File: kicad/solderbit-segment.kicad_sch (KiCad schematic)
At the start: 13 parts, among them J1 Conn_01x05_Pin, U1 PCF8574AT, U2 PCF8574N

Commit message: Update schematic and cleanup
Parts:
- C1: Onecall order code (none) -> 3188966; Package (none) -> 1206
- DS1: value ADMR10A0 -> ADMO10A0; Onecall order code (none) -> 2682705; Package (none) -> 10mm,SMD
- J1: Onecall CN14490 -> (none); Onecall order code (none) -> CN14490; Package (none) -> 2.54mm,THT
- R1, R2, R3, R4, R5, R6, R7, R8: value 220R -> 150R; Onecall order code (none) -> 9240420RL; Package (none) -> 1206
- U1: Onecall 2776146 -> (none); Onecall order code (none) -> 2776146; now not fitted
- U2: Onecall 3124747 -> (none); Onecall order code (none) -> 3124747
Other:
- moved on the sheet: C1, DS1, J1, R1, R2, R3, R4, R5, R6, R7, R8, U2

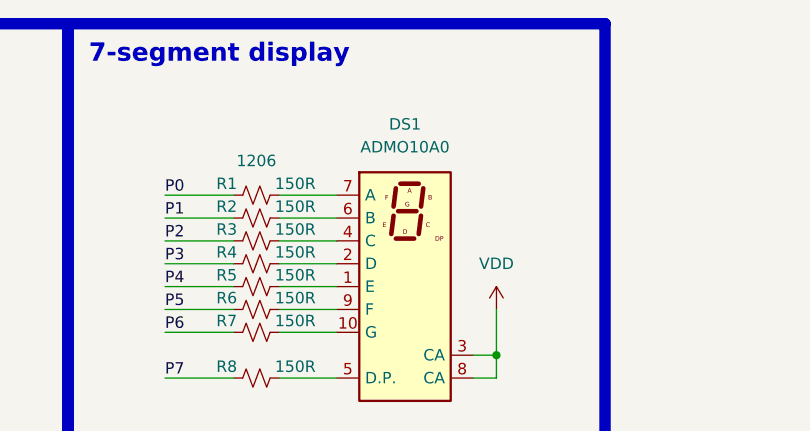
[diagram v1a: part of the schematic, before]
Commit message: Fixed the 7-segment display part number
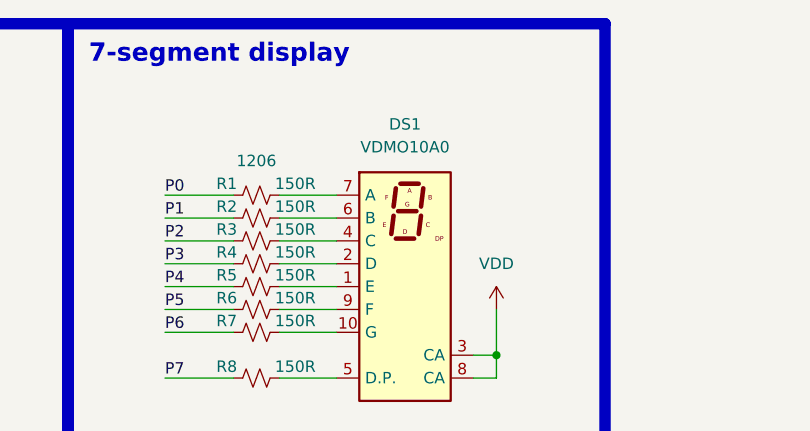
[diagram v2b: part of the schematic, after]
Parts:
- DS1: value ADMO10A0 -> VDMO10A0
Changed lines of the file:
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@@
 			)
 		)
-		(property "Value" "ADMO10A0"
+		(property "Value" "VDMO10A0"
 			(at 180.34 34.036 0)
 			(effects

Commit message: Repo cleanup and library links changes
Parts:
- C1: footprint SolderbitSegment:C_1206 -> Solderbit_Segment:C_1206
- DS1: footprint SolderbitSegment:VDMR10 -> Solderbit_Segment:VDMR10; symbol SolderbitSegment:ADMR10A0 -> Solderbit_Segment:ADMR10A0
- J1: footprint SolderbitSegment:PinHeader_1x05_P2.54mm_Vertical -> Solderbit_Segment:PinHeader_1x05_P2.54mm_Vertical
- R1, R2, R3, R4, R5, R6, R7, R8: footprint SolderbitSegment:R_1206 -> Solderbit_Segment:R_1206
- U1: footprint SolderbitSegment:SO-16 -> Solderbit_Segment:SO-16
- U2: footprint SolderbitSegment:DIP-16 -> Solderbit_Segment:DIP-16
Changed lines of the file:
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@@
 			)
 		)
-		(property "Footprint" "SolderbitSegment:R_1206"
+		(property "Footprint" "Solderbit_Segment:R_1206"
 			(at 163.83 59.69 0)
 			(effects
@@
 			)
 		)
-		(property "Footprint" "SolderbitSegment:R_1206"
+		(property "Footprint" "Solderbit_Segment:R_1206"
 			(at 163.83 54.61 0)
 			(effects
@@
 			)
 		)
-		(property "Footprint" "SolderbitSegment:R_1206"
+		(property "Footprint" "Solderbit_Segment:R_1206"
 			(at 163.83 46.99 0)
 			(effects
@@
 			)
 		)
-		(property "Footprint" "SolderbitSegment:R_1206"
+		(property "Footprint" "Solderbit_Segment:R_1206"
 			(at 163.83 44.45 0)
 			(effects
@@
 			)
 		)
-		(property "Footprint" "SolderbitSegment:R_1206"
+		(property "Footprint" "Solderbit_Segment:R_1206"
 			(at 163.83 52.07 0)
 			(effects
@@
 			)
 		)
-		(property "Footprint" "SolderbitSegment:C_1206"
+		(property "Footprint" "Solderbit_Segment:C_1206"
 			(at 111.76 71.12 0)
 			(effects
@@
 			)
 		)
-		(property "Footprint" "SolderbitSegment:R_1206"
+		(property "Footprint" "Solderbit_Segment:R_1206"
 			(at 163.83 49.53 0)
 			(effects
@@
 			)
 		)
-		(property "Footprint" "SolderbitSegment:SO-16"
+		(property "Footprint" "Solderbit_Segment:SO-16"
 			(at 45.72 72.39 0)
 			(effects
@@
 			)
 		)
-		(property "Footprint" "SolderbitSegment:DIP-16"
+		(property "Footprint" "Solderbit_Segment:DIP-16"
 			(at 86.36 72.39 0)
 			(effects
@@
 			)
 		)
-		(property "Footprint" "SolderbitSegment:R_1206"
+		(property "Footprint" "Solderbit_Segment:R_1206"
 			(at 163.83 41.91 0)
 			(effects
@@
 	)
 	(symbol
-		(lib_id "SolderbitSegment:ADMR10A0")
+		(lib_id "Solderbit_Segment:ADMR10A0")
 		(at 180.34 49.53 0)
 		(unit 1)
@@
 			)
 		)
-		(property "Footprint" "SolderbitSegment:VDMR10"
+		(property "Footprint" "Solderbit_Segment:VDMR10"
 			(at 167.64 67.31 0)
 			(effects
@@
 			)
 		)
-		(property "Footprint" "SolderbitSegment:PinHeader_1x05_P2.54mm_Vertical"
+		(property "Footprint" "Solderbit_Segment:PinHeader_1x05_P2.54mm_Vertical"
 			(at 180.34 109.22 0)
 			(effects
@@
 			)
 		)
-		(property "Footprint" "SolderbitSegment:R_1206"
+		(property "Footprint" "Solderbit_Segment:R_1206"
 			(at 163.83 39.37 0)
 			(effects

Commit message: New documentation
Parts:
- J1: Onecall order code CN14490 -> 3049532
- R1, R2, R3, R4, R5, R6, R7, R8: Onecall order code 9240420RL -> 9240420
- U1: now fitted
- U2: now not fitted
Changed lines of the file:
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@@
 			)
 		)
-		(property "Onecall order code" "9240420RL"
+		(property "Onecall order code" "9240420"
+			(at 163.83 59.69 90)
+			(effects
+				(font
+					(size 1.27 1.27)
+				)
+				(hide yes)
+			)
+		)
+		(property "LCSC Part" ""
 			(at 163.83 59.69 90)
 			(effects
@@
 			)
 		)
-		(property "Onecall order code" "9240420RL"
+		(property "Onecall order code" "9240420"
+			(at 163.83 54.61 90)
+			(effects
+				(font
+					(size 1.27 1.27)
+				)
+				(hide yes)
+			)
+		)
+		(property "LCSC Part" ""
 			(at 163.83 54.61 90)
 			(effects
@@
 			)
 		)
-		(property "Onecall order code" "9240420RL"
+		(property "Onecall order code" "9240420"
+			(at 163.83 46.99 90)
+			(effects
+				(font
+					(size 1.27 1.27)
+				)
+				(hide yes)
+			)
+		)
+		(property "LCSC Part" ""
 			(at 163.83 46.99 90)
 			(effects
@@
 			)
 		)
-		(property "Onecall order code" "9240420RL"
+		(property "Onecall order code" "9240420"
+			(at 163.83 44.45 90)
+			(effects
+				(font
+					(size 1.27 1.27)
+				)
+				(hide yes)
+			)
+		)
+		(property "LCSC Part" ""
 			(at 163.83 44.45 90)
 			(effects
@@
 			)
 		)
-		(property "Onecall order code" "9240420RL"
+		(property "Onecall order code" "9240420"
+			(at 163.83 52.07 90)
+			(effects
+				(font
+					(size 1.27 1.27)
+				)
+				(hide yes)
+			)
+		)
+		(property "LCSC Part" ""
 			(at 163.83 52.07 90)
 			(effects
@@
 			)
 		)
+		(property "LCSC Part" ""
+			(at 111.76 71.12 0)
+			(effects
+				(font
+					(size 1.27 1.27)
+				)
+				(hide yes)
+			)
+		)
 		(pin "2"
 		)
@@
 			)
 		)
-		(property "Onecall order code" "9240420RL"
+		(property "Onecall order code" "9240420"
+			(at 163.83 49.53 90)
+			(effects
+				(font
+					(size 1.27 1.27)
+				)
+				(hide yes)
+			)
+		)
+		(property "LCSC Part" ""
 			(at 163.83 49.53 90)
 			(effects
@@
 		(in_bom yes)
 		(on_board yes)
-		(dnp yes)
+		(dnp no)
 		(property "Reference" "U1"
 			(at 47.498 54.102 0)
@@
 			)
 		)
+		(property "LCSC Part" ""
+			(at 45.72 72.39 0)
+			(effects
+				(font
+					(size 1.27 1.27)
+				)
+				(hide yes)
+			)
+		)
 		(pin "12"
 		)
@@
 		(in_bom yes)
 		(on_board yes)
-		(dnp no)
+		(dnp yes)
 		(property "Reference" "U2"
 			(at 88.138 54.102 0)
@@
 		)
 		(property "Onecall order code" "3124747"
+			(at 86.36 72.39 0)
+			(effects
+				(font
+					(size 1.27 1.27)
+				)
+				(hide yes)
+			)
+		)
+		(property "LCSC Part" ""
 			(at 86.36 72.39 0)
 			(effects
@@
 			)
 		)
-		(property "Onecall order code" "9240420RL"
+		(property "Onecall order code" "9240420"
+			(at 163.83 41.91 90)
+			(effects
+				(font
+					(size 1.27 1.27)
+				)
+				(hide yes)
+			)
+		)
+		(property "LCSC Part" ""
 			(at 163.83 41.91 90)
 			(effects
@@
 			)
 		)
-		(property "Datasheet" "https://4donline.ihs.com/images/VipMasterIC/IC/VISH/VISH-S-A0001108912/VISH-S-A0001108912-1.pdf"
+		(property "Datasheet" "https://www.vishay.com/docs/84196/vdmx10x0.pdf"
 			(at 128.778 30.988 0)
 			(effects
@@
 			)
 		)
+		(property "LCSC Part" ""
+			(at 180.34 49.53 0)
+			(effects
+				(font
+					(size 1.27 1.27)
+				)
+				(hide yes)
+			)
+		)
 		(pin "4"
 		)
@@
 			)
 		)
-		(property "Onecall order code" "CN14490"
+		(property "Onecall order code" "3049532"
+			(at 180.34 109.22 0)
+			(effects
+				(font
+					(size 1.27 1.27)
+				)
+				(hide yes)
+			)
+		)
+		(property "LCSC Part" ""
 			(at 180.34 109.22 0)
 			(effects
@@
 			)
 		)
-		(property "Onecall order code" "9240420RL"
+		(property "Onecall order code" "9240420"
 			(at 163.83 39.37 90)
 			(effects
+				(font
+					(size 1.27 1.27)
+				)
+				(hide yes)
+			)
+		)
+		(property "LCSC Part" ""
+			(at 163.83 39.37 90)
+			(effects

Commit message: Update documentation
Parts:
- DS1: LCSC Part (none) -> C2913076; LCSC datasheet (none) -> https://www.lcsc.com/datasheet/C2913076.pdf; Onecall (none) -> 2682705; Onecall order code 2682705 -> (none); Package 10mm,SMD -> SMD; Type (none) -> Extended
- U1: Onecall (none) -> 2776146; Onecall order code 2776146 -> (none)
- U2: Onecall (none) -> 3124747; Onecall order code 3124747 -> (none)
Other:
- title: solder:bit Segment -> ${PROJECTNAME}
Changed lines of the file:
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@@
 	(paper "A4")
 	(title_block
-		(title "solder:bit Segment")
+		(title "${PROJECTNAME}")
 		(date "2026-02-16")
 		(rev "v0.1")
@@
 		)
 		(property "Package" "SO-16"
-			(at 50.8 58.928 0)
-			(effects
-				(font
-					(size 1.27 1.27)
-				)
-			)
-		)
-		(property "Onecall order code" "2776146"
-			(at 45.72 72.39 0)
-			(effects
-				(font
-					(size 1.27 1.27)
-				)
-				(hide yes)
-			)
-		)
-		(property "LCSC Part" ""
+			(at 51.054 58.928 0)
+			(effects
+				(font
+					(size 1.27 1.27)
+				)
+			)
+		)
+		(property "Onecall" "2776146"
 			(at 45.72 72.39 0)
 			(effects
@@
 			)
 		)
-		(property "Onecall order code" "3124747"
-			(at 86.36 72.39 0)
-			(effects
-				(font
-					(size 1.27 1.27)
-				)
-				(hide yes)
-			)
-		)
-		(property "LCSC Part" ""
+		(property "Onecall" "3124747"
 			(at 86.36 72.39 0)
 			(effects
@@
 			)
 		)
-		(property "Package" "10mm,SMD"
+		(property "Package" "SMD"
 			(at 180.34 34.544 0)
 			(effects
@@
 			)
 		)
-		(property "Onecall order code" "2682705"
+		(property "Onecall" "2682705"
 			(at 180.34 49.53 0)
 			(effects
@@
 			)
 		)
-		(property "LCSC Part" ""
+		(property "LCSC Part" "C2913076"
+			(at 180.34 49.53 0)
+			(effects
+				(font
+					(size 1.27 1.27)
+				)
+				(hide yes)
+			)
+		)
+		(property "Type" "Extended"
+			(at 180.34 49.53 0)
+			(effects
+				(font
+					(size 1.27 1.27)
+				)
+				(hide yes)
+			)
+		)
+		(property "LCSC datasheet" "https://www.lcsc.com/datasheet/C2913076.pdf"
 			(at 180.34 49.53 0)
 			(effects
@@
 			(at 180.34 109.22 0)
 			(effects
-				(font
-					(size 1.27 1.27)
-				)
-				(hide yes)
-			)
-		)
-		(property "LCSC Part" ""
-			(at 180.34 109.22 0)
-			(effects
